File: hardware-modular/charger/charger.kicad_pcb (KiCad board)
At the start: 2 copper layers, 100 x 60 mm, 69 parts, among them J1 DC_IN, J2 Pickit 2, J3 BAT_OUT_4, J4 BAT_OUT_1, J5 BAT_OUT_2, J6 BAT_OUT_3, Q1 IRF9510, Q2 BD137, Q3 BD137, Q4 BD137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

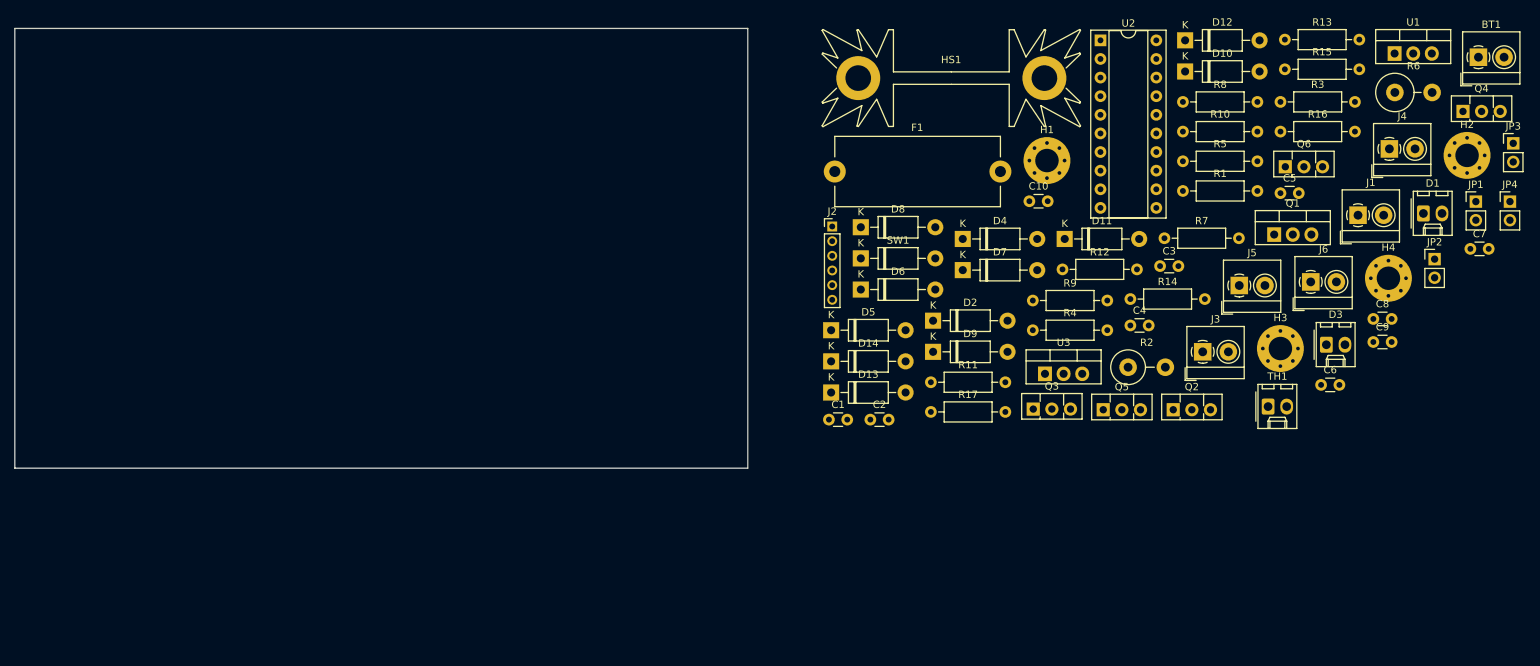
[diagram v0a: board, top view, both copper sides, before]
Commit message: Li-Po charger module - PCB.
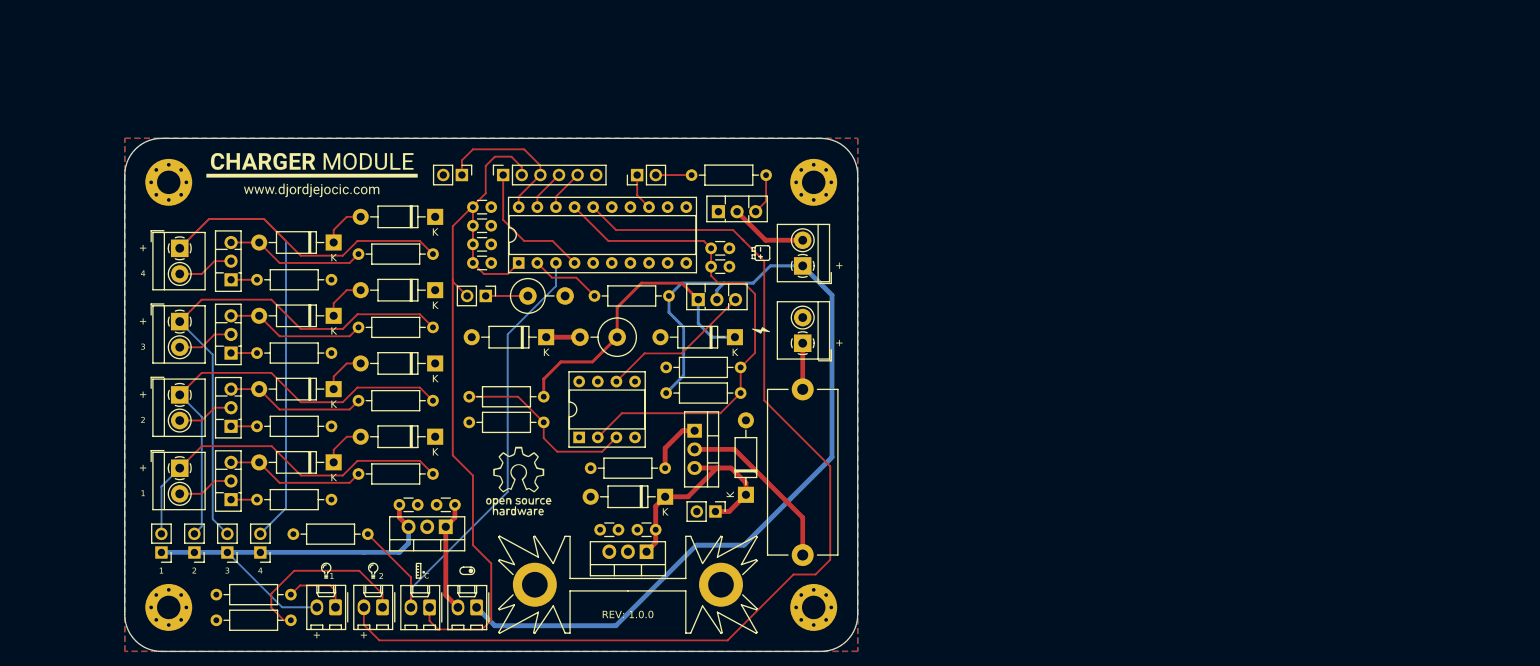
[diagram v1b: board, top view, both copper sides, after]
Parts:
- added G***: LOGO, Icons:Charger_Module_Label, F.Cu at (80.5, 50.0)
- added G***: OSHW LOGO, Icons:OSHW, F.Cu at (108.8, 91.8)
- added G***: Switch, Icons:Switch, F.Cu at (101.7, 104.0)
- added G***: Thermometer, Icons:Thermometer, F.Cu at (95.1, 104.0)
- added G***: Lightbulb, Icons:Lightbulb, F.Cu at (88.9, 104.0)
- added G***: Lightbulb, Icons:Lightbulb, F.Cu at (82.5, 104.0)
- added G***: Lightning, Icons:Lightning, F.Cu at (142.0, 71.2)
- added G***: Battery, Icons:Battery, F.Cu at (142.0, 60.6)
- added JP5: Jumper, Connector_PinHeader_2.54mm:PinHeader_1x02_P2.54mm_Vertical, F.Cu at (60.0, 101.5)
- added JP6: Jumper, Connector_PinHeader_2.54mm:PinHeader_1x02_P2.54mm_Vertical, F.Cu at (64.5, 101.5)
- added JP7: Jumper, Connector_PinHeader_2.54mm:PinHeader_1x02_P2.54mm_Vertical, F.Cu at (69.0, 101.5)
- added JP8: Jumper, Connector_PinHeader_2.54mm:PinHeader_1x02_P2.54mm_Vertical, F.Cu at (73.5, 101.5)
- added Q7: BD137, Package_TO_SOT_THT:TO-126-3_Vertical, F.Cu at (136.0, 55.0)
- added R18: 220, Resistor_THT:R_Axial_DIN0207_L6.3mm_D2.5mm_P10.16mm_Horizontal, F.Cu at (102.0, 80.2)
- added R19: 10, Resistor_THT:R_Axial_DIN0207_L6.3mm_D2.5mm_P10.16mm_Horizontal, F.Cu at (102.0, 83.8)
- added R20: 100, Resistor_THT:R_Axial_DIN0207_L6.3mm_D2.5mm_P10.16mm_Horizontal, F.Cu at (129.2, 66.5)
- added U4: LM741, Package_DIP:DIP-8_W7.62mm_Socket, F.Cu at (117.0, 85.8)
- C10: value 0.33μF -> 0.1μF
- J2: footprint Connector_PinHeader_2.00mm:PinHeader_1x06_P2.00mm_Vertical -> Connector_PinSocket_2.54mm:PinSocket_1x06_P2.54mm_Vertical
- Q3: value BD137 -> BD136
- R3: value 270 -> 220
- SW1: footprint Diode_THT:D_DO-41_SOD81_P10.16mm_Horizontal -> Connector_Molex:Molex_KK-254_AE-6410-02A_1x02_P2.54mm_Vertical
- moved Q4 176.2 mm to (69.5, 94.3), turned to 90 degrees
- moved H4 172.4 mm to (61.0, 109.0)
- moved J4 170.7 mm to (62.5, 90.0), turned to 270 degrees
- moved R3 160.0 mm to (67.5, 107.2)
- moved J6 154.4 mm to (62.5, 70.0), turned to 270 degrees
- moved D1 151.8 mm to (90.2, 109.0), turned to 180 degrees
- moved Q6 146.1 mm to (69.5, 74.3), turned to 90 degrees
- moved J5 145.3 mm to (62.5, 80.0), turned to 270 degrees
- moved R1 144.3 mm to (67.5, 110.8)
- moved JP3 143.5 mm to (101.0, 50.0), turned to 270 degrees
- moved R15 142.7 mm to (83.2, 94.3), turned to 180 degrees
- moved J3 140.3 mm to (62.5, 60.0), turned to 270 degrees
- moved D3 139.9 mm to (83.8, 109.0), turned to 180 degrees
- moved R16 135.6 mm to (83.2, 84.3), turned to 180 degrees
- moved R5 131.6 mm to (78.0, 99.0)
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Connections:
- C1 pad 1: Net-(C1-Pad1) -> VDD
- C2 pad 1: Net-(C1-Pad1) -> VDD
- C3 pad 1: Net-(C1-Pad1) -> VDD
- C4 pad 1: Net-(C1-Pad1) -> VDD
- D6 pad 1: Net-(BT1-Pad1) -> Net-(D6-Pad1)
- J3 pad 1: BAT -> Net-(J3-Pad1)
- J4 pad 1: BAT -> Net-(J4-Pad1)
- J5 pad 1: BAT -> Net-(J5-Pad1)
- J6 pad 1: BAT -> Net-(J6-Pad1)
- JP2 pad 1: Net-(C1-Pad1) -> Net-(JP2-Pad1)
- Q3 pad 1: GND -> Net-(D6-Pad1)
- Q3 pad 2: Net-(BT1-Pad2) -> Net-(BT1-Pad1)
- R10 pad 2: BAT -> Net-(J4-Pad1)
- R11 pad 2: BAT -> Net-(J5-Pad1)
- R12 pad 2: BAT -> Net-(J6-Pad1)
- R13 pad 1: Net-(Q3-Pad3) -> Net-(Q7-Pad3)
- R2 pad 1: Net-(C1-Pad1) -> Net-(JP2-Pad1)
- R6 pad 1: Net-(BT1-Pad1) -> Net-(D6-Pad1)
- R9 pad 2: BAT -> Net-(J3-Pad1)
- U2 pad 2: Net-(U2-Pad2) -> PROBE
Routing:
- net STS: track 0.00 -> 142.7 mm
- net Net-(BT1-Pad1): track 0.00 -> 124.5 mm
- net VDD: track 0.00 -> 102.7 mm
- net Net-(J3-Pad1): track 0.00 -> 98.7 mm
- net Net-(J6-Pad1): track 0.00 -> 70.7 mm
- net REF: track 0.00 -> 68.1 mm
- net TEMP: track 0.00 -> 67.6 mm
- net Net-(J5-Pad1): track 0.00 -> 59.6 mm
- net BAT: track 0.00 -> 55.3 mm
- net Net-(J4-Pad1): track 0.00 -> 49.0 mm
- net Net-(D6-Pad1): track 0.00 -> 41.4 mm
- net Net-(C5-Pad1): track 0.00 -> 31.8 mm
- net Net-(R18-Pad1): track 0.00 -> 25.3 mm
- net Net-(D1-Pad1): track 0.00 -> 24.9 mm
- net Net-(F1-Pad1): track 0.00 -> 23.7 mm
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- added copper zone on F.Cu, net DC
- added copper zone on B.Cu, net GND
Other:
- board size 100 x 60 mm -> 100 x 70 mm
- board text added: "+"
- board text added: "1"
- board text added: "2"
- board text added: "3"
- board text added: "4"
- board text added: "REV: 1.0.0"

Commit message: Gerber files - Charger.
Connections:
- net SWITCH renamed Net-(U2-Pad15)
